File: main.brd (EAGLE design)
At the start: 78 x 235 mm, 117 parts, among them IC1 FXAS21000, IC2 ADXL343BCCZ, IC3 MPL3115A2LGA, IC4 FGPMMOPA6H, IC5 25LC1024-I/P, Q1 MCP9700A-E/TO, Q2 MCP9700A-E/TO, Q3 12MHz, Q4 FQP7P06, U1 ATMEGA1284P-PU, U2 LT3570EFEPBF, U3 TL431BQLP, X1 132134RP

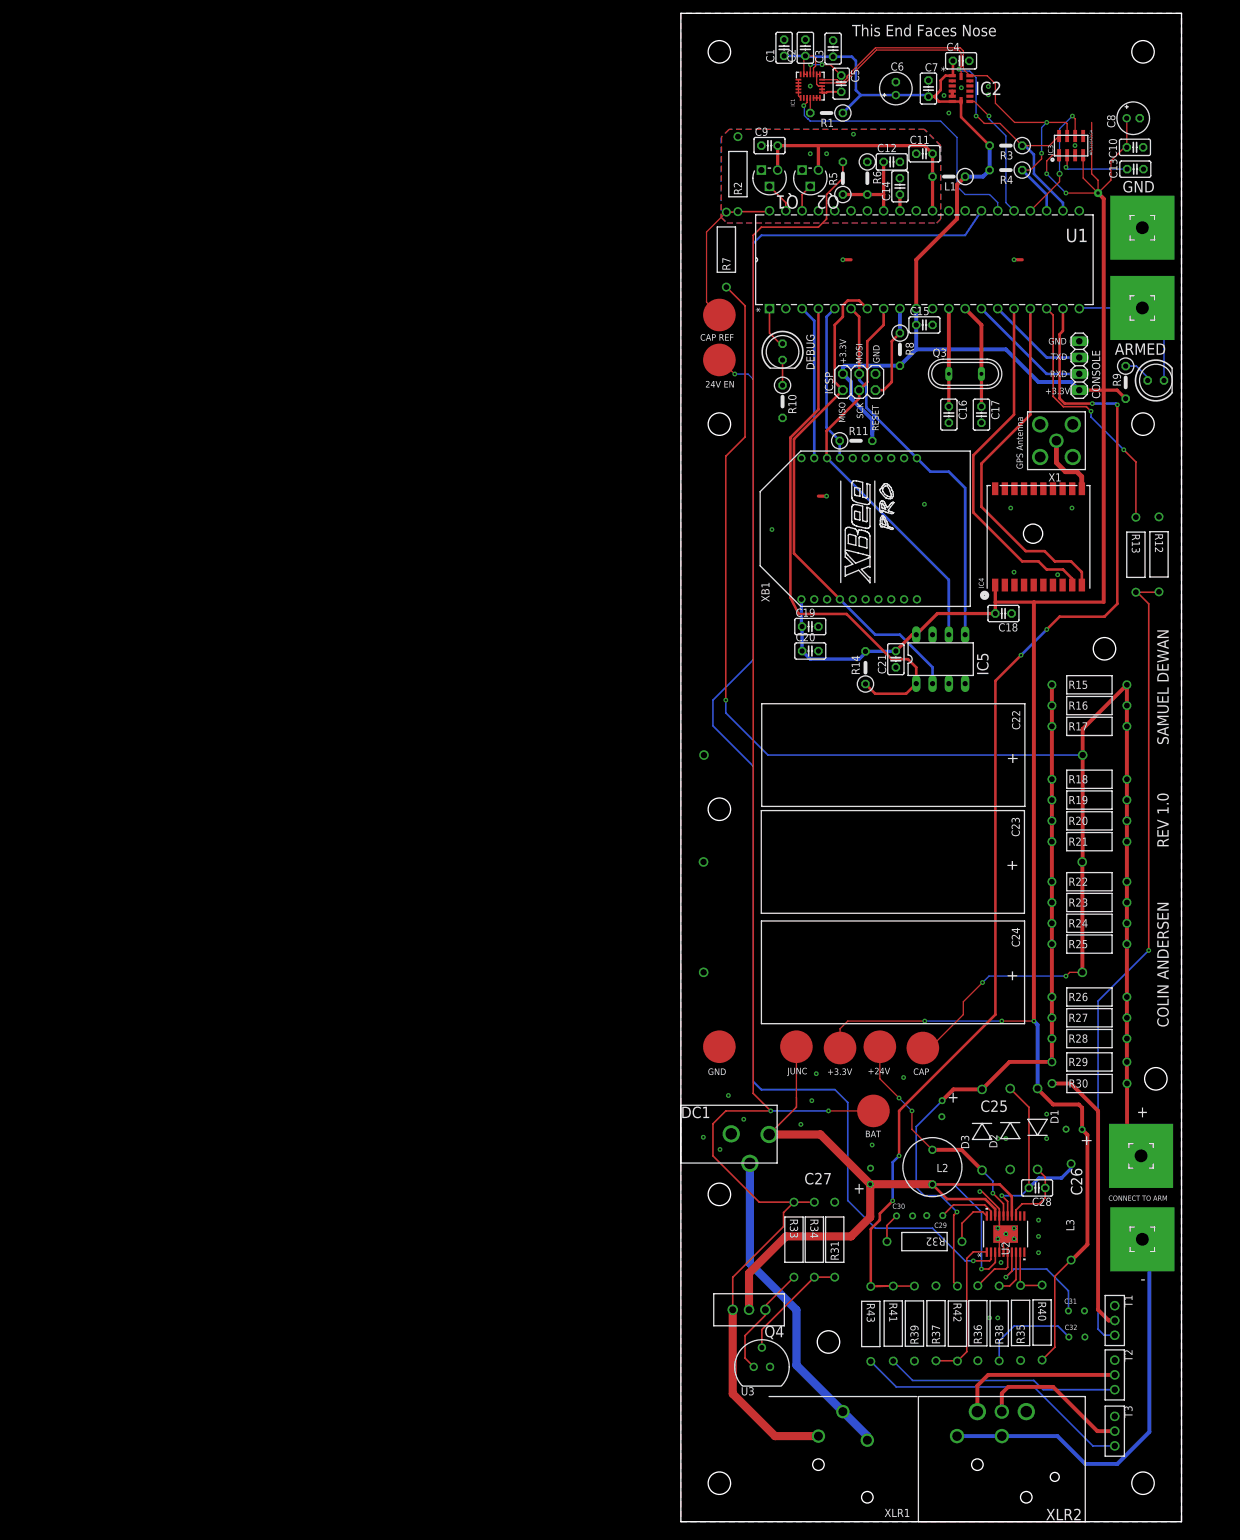
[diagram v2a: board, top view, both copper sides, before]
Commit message: Relayed-out digital section.
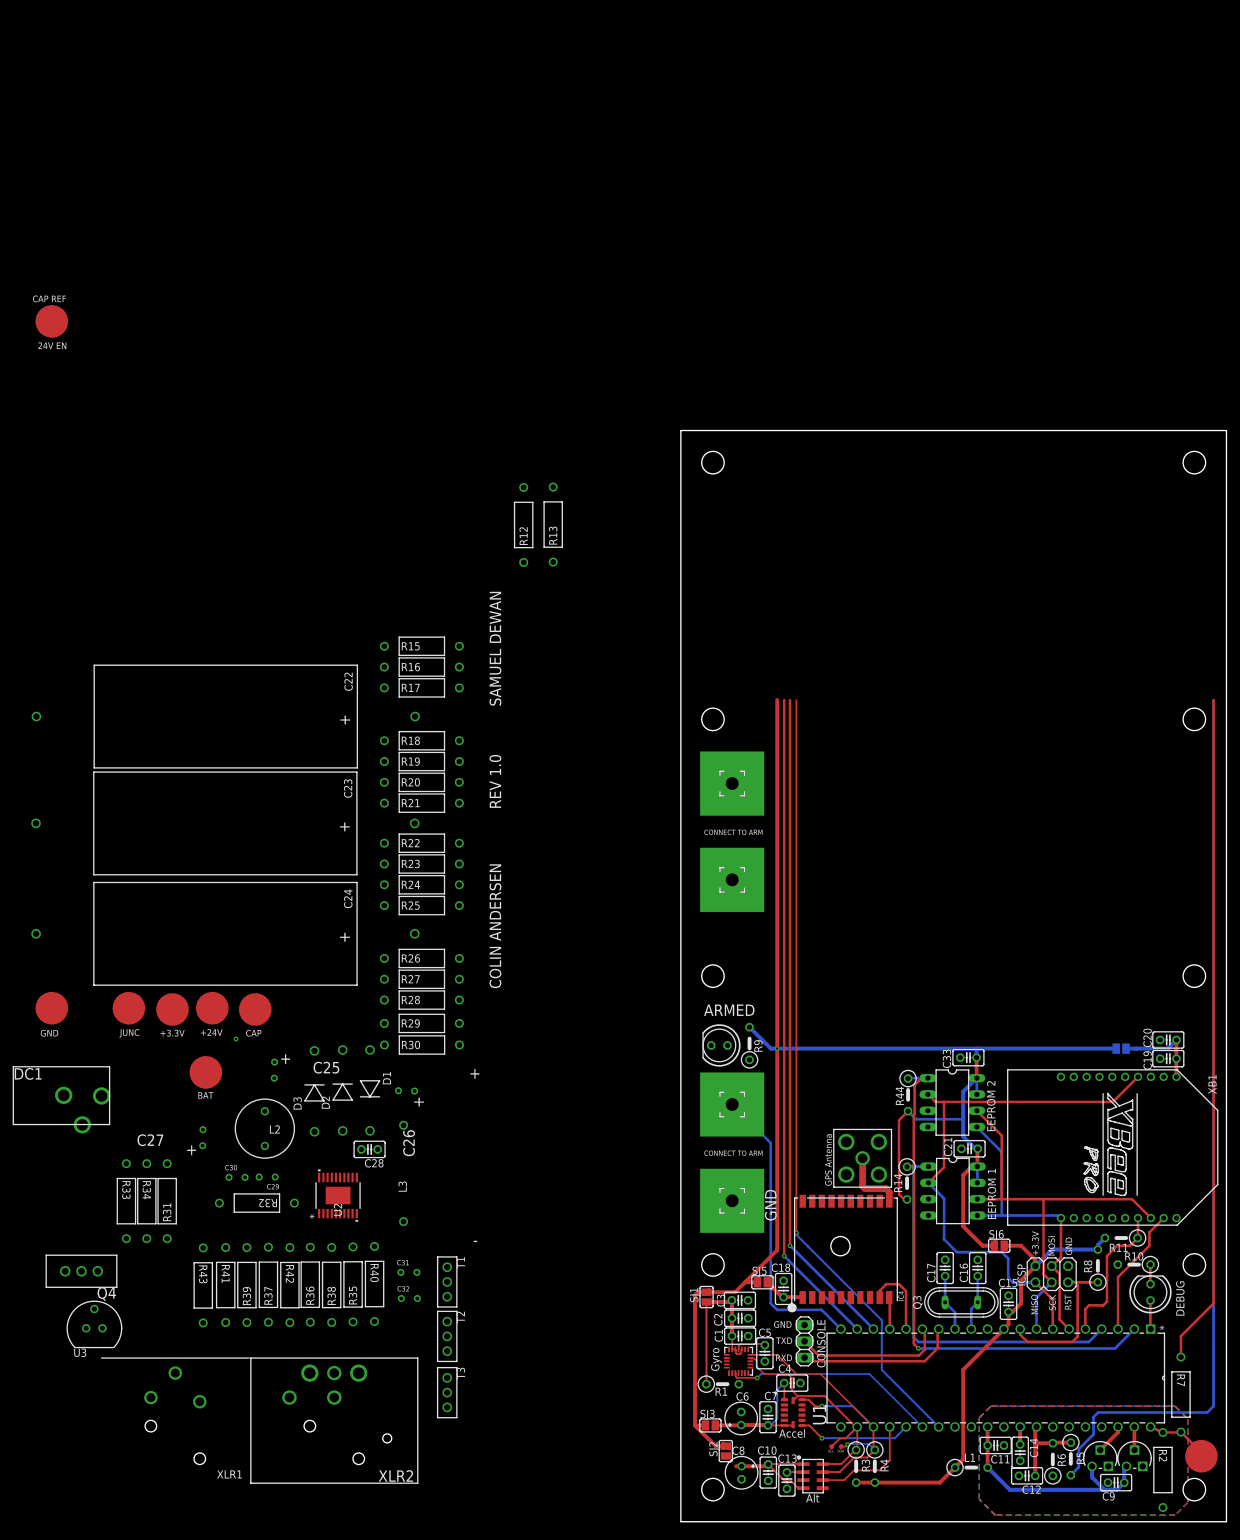
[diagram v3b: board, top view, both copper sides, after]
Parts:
- added C33: 0.1µF, rcl:C025-025X050
- added IC6: 25LC1024-I/P, microchip:DIL8
- added R44: 1MΩ, rcl:0207/5V
- added SCL, SDA: TEST-POINT3, SparkFun-Connectors:PAD.03X.03
- added SJ1, SJ2, SJ3, SJ4, SJ5, SJ6: (no value), jumper:SJ
- CONSOLE: device pinhead:1X04 -> pinhead:1X03
- R10: value 2K2Ω -> 1KΩ
- R3, R4: value 4k7Ω -> 2k2Ω
- R9: value 2K2Ω -> 180Ω
- moved R2 223.6 mm to (75.1, 2.21), turned to 270 degrees
- moved C8 219.7 mm to (9.46, 7.63), turned to 270 degrees
- moved C9 215.2 mm to (67.8, 6.09)
- moved C10 214.2 mm to (13.6, 7.65), turned to 270 degrees
- moved C13 211.4 mm to (16.5, 6.40), turned to 270 degrees
- moved IC3 211.2 mm to (20.6, 7.10), turned to 0 degrees
- moved C6 208.6 mm to (9.39, 16.1)
- moved C7 208.5 mm to (13.6, 16.3)
- moved IC2 207.9 mm to (17.5, 17.0)
- moved C4 207.7 mm to (17.4, 21.6)
- moved R3 207.1 mm to (27.3, 8.64), turned to 270 degrees
- moved C12 205.8 mm to (53.9, 7.15), turned to 180 degrees
- moved Q1 205.7 mm to (72.0, 11.2), turned to 0 degrees
- moved R4 203.0 mm to (30.2, 8.64), turned to 270 degrees
- moved R7 202.8 mm to (77.9, 14.0), turned to 270 degrees
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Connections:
- new net EEPROM2_CS: IC6.1, R44.1, U1.2
- new net RELAY_ARM: U1.27
- new net VCC_ACCEL: C4.1, C6.+, C7.1, IC2.1, IC2.6, IC2.7, SJ3.2
- new net VCC_ALT: C10.1, C8.+, IC3.P$1, IC3.P$4, SJ2.2
- new net VCC_GPS: C18.2, IC4.P$1, SJ5.2
- new net VCC_GYRO: C1.1, C2.1, C3.1, IC1.15, IC1.17, IC1.18, R1.1, SJ1.2
- new net VCC_MCU: C15.1, ICSP.2, L1.1, R11.2, R3.2, R4.2, R8.2, SJ6.2, U1.10
- new net VCC_XB: C19.1, C20.1, SJ4.2, XB1.1
- net 12V_ENABLE: no longer U1.27
- net GND: now also C33.2, CONSOLE.3, IC6.3, IC6.4; no longer CONSOLE.4, IC5.7
- net MISO: now also IC6.2
- net MOSI: now also IC6.5
- net RXD0: now also CONSOLE.1; no longer CONSOLE.2
- net SCK: now also IC6.6
- net SCL: now also SCL.P$1
- net SDA: now also SDA.P$1
- net TXD0: now also CONSOLE.2; no longer CONSOLE.3
- net VCC: now also C33.1, IC5.7, IC6.7, IC6.8, R44.2, SJ1.1, SJ2.1, SJ3.1, SJ4.1, SJ5.1, SJ6.1; no longer C1.1, C10.1, C15.1, C18.2, C19.1, C2.1, C20.1, C3.1, C4.1, C6.+, C7.1, C8.+, CONSOLE.1, IC1.15, IC1.17, IC1.18, IC2.1, IC2.6, IC2.7, IC3.P$1, IC3.P$4, IC4.P$1, ICSP.2, L1.1, R1.1, R11.2, R3.2, R4.2, R8.2, U1.10, XB1.1
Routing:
- net 12V_ENABLE: track 239.1 -> 0.00 mm, vias 2 -> 0
- net VCC: track 495.7 -> 257.9 mm, vias 6 -> 1
- net N$81: track 280.6 -> 104.5 mm, vias 3 -> 0
- net PWR_JUNC: track 128.6 -> 0.00 mm, vias 1 -> 0
- net N$82: track 125.7 -> 0.00 mm, vias 1 -> 0
- net RELAY_ARM: track 0.00 -> 122.4 mm, vias 0 -> 1
- net BAT+: track 259.5 -> 139.9 mm, vias 2 -> 0
- net +12.0: track 113.5 -> 0.00 mm, vias 1 -> 0
- net MAIN_TRIGGER: track 191.3 -> 102.7 mm, vias 6 -> 1
- net EEPROM2_CS: track 0.00 -> 81.9 mm, vias 0 -> 1
- net VCC_MCU: track 0.00 -> 73.1 mm
- net N$31: track 64.3 -> 0.00 mm
- net CAP_DISCHARGE: track 40.4 -> 103.4 mm, vias 2 -> 1
- net TXD1: track 55.9 -> 4.95 mm
- net N$30: track 50.7 -> 0.00 mm
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- removed copper zone on layer 1, net GND
- removed copper zone on layer 16, net GND
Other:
- board size 78 x 235 mm -> 85 x 170 mm
- board text added: "Accel"
- board text added: "Alt"
- board text added: "EEPROM 1"
- board text added: "EEPROM 2"
- board text added: "Gyro"
- board text added: "RST"
- board text added: "SCL"
- board text added: "SDA"
- board text removed: "RESET"
- board text removed: "This End Faces Nose"

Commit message: Update
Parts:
- removed ARMED: RED, led:LED5MM
- removed DC1: PJ-102BH, Power:DC_JACK_3
- removed PAD4: (no value), Power:3,81/1,4
- removed SJ6: (no value), jumper:SJ
- removed U$8: BAT+, Power:TEST
- added ARMED1, ARMED2: RED, led:LED5MM
- added C34: 10µF, rcl:E2-5
- added C35, C36, C37: 0.1µF, rcl:C025-025X050
- added Q5: MCP9700A-E/TO, CU in Space:TO127P254X533-3
- added R45, R48: (no value), rcl:0207/5V
- added R46, R47: 47kΩ, rcl:0207/5V
- added R49, R50: 2k2Ω, rcl:0207/5V
- added SJ200: (no value), jumper:SJ
- added T4: (no value), Power:NPNDARL
- C1, C14, C2: value 0.1µF -> 22µF; device rcl:C025-025X050 -> Power:2.5MM_AL_CAP
- C11, C4: value 0.1µF -> 338TTA035M; device rcl:C025-025X050 -> Power:338TTA035M
- C12: value 0.1µF -> SNUB
- C13, C3, C7: value 0.1µF -> 10 uF; device rcl:C025-025X050 -> Power:2.5MM_CAP
- C15: value 2.2µF -> 338TTA035M; device rcl:C025-025X050 -> Power:338TTA035M
- C16: value 27pF -> 1µF
- C17: value 27pF -> 0.1µF
- C18: value 0.1µF -> 47pF
- C19: value 47pF -> 0.1µF
- C20: value 1µF -> 27pF
- C21: value 0.1µF -> 27pF
- C22, C23: value 338TTA035M -> 0.1µF; device Power:338TTA035M -> rcl:C025-025X050
- C24: value 338TTA035M -> 2.2µF; device Power:338TTA035M -> rcl:C025-025X050
- C25, C26, C27: value 22µF -> 0.1µF; device Power:2.5MM_AL_CAP -> rcl:C025-025X050
- C29, C31: value 10nF -> 0.1µF; device Power:2.5MM_CAP -> rcl:C025-025X050
- C30: value 1nF -> 10µF; device Power:2.5MM_CAP -> rcl:E2-5
- C32: value 1nF -> 0.1µF; device Power:2.5MM_CAP -> rcl:C025-025X050
- C5, C9: value 0.1µF -> 1nF; device rcl:C025-025X050 -> Power:2.5MM_CAP
- C6, C8: value 10µF -> 10nF; device rcl:E2-5 -> Power:2.5MM_CAP
- IC1: value FXAS21000 -> 25LC1024-I/P; device Freescale_Sensors_v2:QFN24_0P5_4X4_ASYM_EXP -> microchip:DIL8
- IC2: value ADXL343BCCZ -> 25LC1024-I/P; device CU in Space:LGA14R80P1X6_300X500X100 -> microchip:DIL8
- IC3: value MPL3115A2LGA -> FGPMMOPA6H; device microbuilder:LGA8 -> microbuilder:FGPMMOPA6H
- IC4: value FGPMMOPA6H -> FXAS21000; device microbuilder:FGPMMOPA6H -> Freescale_Sensors_v2:QFN24_0P5_4X4_ASYM_EXP
- IC5: value 25LC1024-I/P -> ADXL343BCCZ; device microchip:DIL8 -> CU in Space:LGA14R80P1X6_300X500X100
- IC6: value 25LC1024-I/P -> MPL3115A2LGA; device microchip:DIL8 -> microbuilder:LGA8
- L1: value 10µH -> 18µH; device rcl:0207/5V -> Power:5.4MM_L
- L3: value 4.7µH -> 10µH; device Power:14MM_L -> rcl:0207/5V
- Q1, Q2: value MCP9700A-E/TO -> FQP7P06; device CU in Space:TO127P254X533-3 -> Power:PMOS
- Q4: value FQP7P06 -> MCP9700A-E/TO; device Power:PMOS -> CU in Space:TO127P254X533-3
- R1: value 47kΩ -> 3.65 kΩ
- R10: value 1KΩ -> 51.1 kΩ
- R11: value 1MΩ -> BOOSTR
- R12: value 1M -> 1.2 k; device Power:YAG_MF25 -> rcl:0207/5V
- R13: value 3.6k -> SNUB; device Power:YAG_MF25 -> rcl:0207/5V
- R14: value 1MΩ -> 3.6k
- R15: value 750 -> 1.2 k; device Power:YAG_MF25 -> rcl:0207/5V
- R16: value 750 -> 3.6 k; device Power:YAG_MF25 -> rcl:0207/5V
- R17, R19: value 750 -> 1 M; device Power:YAG_MF25 -> rcl:0207/5V
- R18: value 750 -> 3.6 K; device Power:YAG_MF25 -> rcl:0207/5V
- R2: value (none) -> 1 MΩ; device Power:YAG_MF25 -> rcl:0207/5V
- R20: value 750 -> 1.4 k; device Power:YAG_MF25 -> rcl:0207/5V
- R21, R22, R23, R24, R25, R26, R27, R28: value 750 -> (none); device Power:YAG_MF25 -> rcl:0207/5V
- R29: value 750 -> 2M Ω; device Power:YAG_MF25 -> rcl:0207/5V
- R3: value 2k2Ω -> 1 MΩ
- R30: value ~1.4k -> 1MΩ; device Power:YAG_MF25 -> rcl:0207/5V
- R31, R34, R40: value 51.1kΩ -> (none); device Power:YAG_MF25 -> rcl:0207/5V
- R32: value 24.9kΩ -> 1.2 k; device Power:YAG_MF25 -> rcl:0207/5V
- R33: value 3.65kΩ -> 1.2k; device Power:YAG_MF25 -> rcl:0207/5V
- R35: value 17.4kΩ -> (none); device Power:YAG_MF25 -> rcl:0207/5V
- R36: value 8.06kΩ -> (none); device Power:YAG_MF25 -> rcl:0207/5V
- R37: value 3.65kΩ -> 1MΩ; device Power:YAG_MF25 -> rcl:0207/5V
- R38: value 24.9kΩ -> (none); device Power:YAG_MF25 -> rcl:0207/5V
- R39: value 1M -> (none); device Power:YAG_MF25 -> rcl:0207/5V
- R4: value 2k2Ω -> 51.1 kΩ
- R41: value 3.6k -> 1MΩ; device Power:YAG_MF25 -> rcl:0207/5V
- R42: value 51.1kΩ -> 1KΩ; device Power:YAG_MF25 -> rcl:0207/5V
- R43: value 3.6k -> 10kΩ; device Power:YAG_MF25 -> rcl:0207/5V
- R44: value 1MΩ -> 47kΩ
- R5: value 47kΩ -> 373.65 kΩ
- R6: value 47kΩ -> 24.9 kΩ
- R7: value (none) -> 8.06 kΩ; device Power:YAG_MF25 -> rcl:0207/5V
- R8: value 10kΩ -> 24.9 kΩ
- R9: value 180Ω -> 17.4 kΩ
- U$1: value TEST -> BAT+
- U$2: value TEST -> +24V
- U$3: value CAP -> +3.3V
- U$4: value BAT+ -> CAP
- U$5: value +24V -> TEST
- U$6: value +3.3V -> CAP
- U$7: value CAP -> TEST
- U1: value ATMEGA1284P-PU -> TL431BQLP; device Atmel_By_element14_Batch_1-00:DIP254P1524X483-40 -> Power:LP3
- U3: value TL431BQLP -> ATMEGA1284P-PU; device Power:LP3 -> Atmel_By_element14_Batch_1-00:DIP254P1524X483-40
- moved XLR1 186.7 mm to (39.4, 150.5)
- moved XLR2 186.5 mm to (64.1, 150.4)
- moved R2 169.5 mm to (6.00, 157.0), turned to 0 degrees
- moved Q1 162.9 mm to (22.3, 166.3)
- moved Q4 162.4 mm to (66.6, 11.2), turned to 0 degrees
- moved C24 156.9 mm to (51.0, 33.9), turned to 90 degrees
- moved U$7 154.6 mm to (79.1, 27.2), turned to 90 degrees
- moved U1 151.7 mm to (11.1, 165.8), turned to 180 degrees
- moved R5 148.7 mm to (6.00, 148.0), turned to 0 degrees
- moved R3 146.9 mm to (6.00, 154.0), turned to 180 degrees
- moved R6 144.9 mm to (6.00, 145.0), turned to 0 degrees
- moved C9 144.9 mm to (6.70, 137.5), turned to 180 degrees
- moved C22 144.8 mm to (16.0, 36.3)
- moved R4 144.4 mm to (6.00, 151.0), turned to 180 degrees
- moved R7 144.2 mm to (6.00, 139.0), turned to 0 degrees
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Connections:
- removed net ARMED_SENSE: ARMED.K, PAD2.1, U1.20
- removed net N$33: ARMED.A, R9.1
- removed net RELAY_ARM: U1.27
- new net EMATCH_SENSE_1: ARMED1.K, R33.1, U3.20
- new net EMATCH_SENSE_2: ARMED2.K, R32.1, U3.21
- new net N$35: R24.2, T4.3
- new net N$67: C12.1, R13.1
- new net N$75: C10.1, R11.1
- new net N$84: ARMED2.A, R15.2
- new net N$85: ARMED1.A, R12.1
- net +12.0: now also C2.1, C3.1, D1.1, R31.1, R34.1, R35.1, R36.1, R38.1, R39.1, R4.1, R40.1, U$2.P$1; no longer C25.1, D3.1, R15.1, R16.1, R17.1, R18.1, R19.1, R20.1, R21.1, R24.1, R29.1, R42.1
- net 12V_ENABLE: now also R24.1, R29.2, U$5.P$1, U3.27; no longer U$2.P$1
- net ACCEL_INT: now also IC5.8, U3.25; no longer IC2.8, U1.25
- net ALT_INT: now also IC6.P$6, U3.24; no longer IC3.P$6, U1.24
- net AREF: now also C32.1, U3.32; no longer C14.1, U1.32
- net AVCC: now also C31.2, C37.2, L3.2, Q4.1, Q5.1, U3.30; no longer C11.2, C9.2, L1.2, Q1.1, Q2.1, U1.30
- net A_GND: now also C31.1, C32.2, C35.2, C37.1, Q4.3, Q5.3, R47.1, R48.2, U3.31; no longer C11.1, C12.2, C14.2, C9.1, Q1.3, Q2.3, R2.2, R6.1, U1.31
- net BAT+: now also Q1.3, R1.1, R2.1, R46.2, U$1.P$1; no longer Q4.3, R33.1, R34.1, R5.2, U$8.P$1
- net BAT_REF: now also C35.1, R46.1, R47.2, U3.33; no longer C12.1, R5.1, R6.2, U1.33
- net CAP_DISCHARGE: now also R18.1, U3.18; no longer R13.1, U1.18
- net CAP_REF: now also R45.2, R48.1, U$7.P$1, U3.40; no longer R2.1, R7.2, U$1.P$1, U1.40
- net DEBUG_LED: now also U3.1; no longer U1.1
- net EEPROM2_CS: now also IC1.1, R30.1, U3.2; no longer IC6.1, R44.1, U1.2
- net EEPROM_CS: now also IC2.1, R37.1, U3.4; no longer IC5.1, R14.1, U1.4
- net FB1: now also R4.2, R5.1; no longer R37.1, R42.2
- net GND: now also C11.-, C12.2, C14.2, C15.-, C18.2, C22.1, C23.2, C24.2, C28.2, C30.-, C34.-, C36.2, C4.-, C6.2, C8.2, C9.2, IC1.3, IC1.4, IC2.3, IC3.P$12, IC3.P$19, IC3.P$8, IC4.1, IC4.10, IC4.13, IC4.14, IC4.19, IC4.20, IC4.21, IC4.22, IC4.23, IC4.24, IC4.5, IC4.6, IC4.7, IC4.8, IC4.9, IC5.12, IC5.2, IC5.5, IC6.P$3, R17.1, R19.1, R29.1, R3.2, R32.2, R33.2, R42.2, R5.2, R7.1, R9.1, T4.1, U$4.P$1, U1.3, U3.11, XLR1.1, XLR1.3; no longer C10.2, C15.2, C18.1, C22.-, C23.-, C24.-, C30.2, C31.2, C32.2, C4.2, C6.-, C8.-, DC1.2, IC1.1, IC1.10, IC1.13, IC1.14, IC1.19, IC1.20, IC1.21, IC1.22, IC1.23, IC1.24, IC1.5, IC1.6, IC1.7, IC1.8, IC1.9, IC2.12, IC2.2, IC2.5, IC4.P$12, IC4.P$19, IC4.P$3, IC4.P$8, IC5.3, IC6.3, IC6.4, PAD1.1, R10.2, R12.1, R31.2, R35.1, R36.1, R37.2, R39.1, U$3.P$1, U1.11, U3.3
- net GPS_FIX: now also IC3.P$5; no longer IC4.P$5
- net GYRO_INT: now also IC4.3, U3.26; no longer IC1.3, U1.26
- net MAIN_TRIGGER: now also R14.1, R16.1, R17.2, U3.19; no longer R39.2, R41.1, R43.1, U1.19
- net MISO: now also IC1.2, IC2.2, U3.7; no longer IC5.2, IC6.2, U1.7
- net MOSI: now also IC1.5, IC2.5, U3.6; no longer IC5.5, IC6.5, U1.6
- net N$1: now also C27.1, IC4.16; no longer C5.1, IC1.16
- net N$10: now also C9.1, R8.1; no longer C32.1, R38.1
- net N$11: now also R6.1; no longer R32.1
- net N$12: now also C6.1; no longer C29.1
- net N$13: now also C10.2, L2.1, R13.2; no longer C28.2, L3.1
- net N$15: now also R10.1, R9.2; no longer R35.2, R40.1
- net N$16: now also D3.1, R11.2; no longer C28.1, D1.1
- net N$2: now also IC4.4, R44.2; no longer IC1.4, R1.2
- net N$3: now also C36.1, IC6.P$2; no longer C13.1, IC3.P$2
- net N$30: now also Q2.3, R21.1, R22.2, R23.2, R25.2, R26.2, R27.2, R28.2, R31.2, R34.2, R35.2, R36.2, R38.2, R39.2, R40.2; no longer DC1.3, XLR1.1, XLR1.3
- net N$31: now also Q2.1, R21.2, T4.2; no longer PAD4.1, XLR2.1, XLR2.3
- net N$34: now also R20.2, T3.2; no longer R30.1, T1.2
- net N$4: now also IC3.P$11; no longer IC4.P$11
- net N$5: now also C8.1; no longer C31.1
- net N$6: now also R7.2; no longer R36.2
- net N$69: now also Q1.1, R1.2, U1.1; no longer Q4.1, R33.2, U3.1
- net N$7: now also R8.2; no longer R38.2
- net N$70: now also R2.2, R3.1, U1.2; no longer R31.1, R34.2, U3.2
- net N$71: now also R42.1; no longer R10.1
- net N$77: now also PAD3.1, R15.1, T1.2, XLR2.4; no longer T3.2, XLR2.2
- net N$78: now also PAD2.1, R12.2, XLR2.3; no longer XLR2.4
- net N$79: now also R16.2, T2.3; no longer R43.2, T3.3
- net N$8: now also D1.2, L1.2; no longer D3.2, L2.2, U$5.P$1
- net N$80: now also R14.2, T1.3; no longer R41.2, T2.3
- net N$81: now also C11.+, C15.+, C4.+, PAD1.1, Q2.2, R20.1, R45.1, U$6.P$1, XLR2.1, XLR2.2; no longer C22.+, C23.+, C24.+, PAD3.1, R15.2, R16.2, R17.2, R18.2, R19.2, R20.2, R21.2, R22.2, R23.2, R24.2, R25.2, R26.2, R27.2, R28.2, R29.2, R30.2, R7.1, U$7.P$1
- net N$82: now also R18.2, R19.2, T3.3; no longer R12.2, R13.2, T1.3
- net N$9: now also C5.1, R6.2; no longer C30.1, R32.2
- net PWR_JUNC: now also C1.1, C7.1, L1.1, Q1.2; no longer C27.1, DC1.1, L2.1, Q4.2, U$4.P$1
- net RADIO_CS: now also R41.1, U3.5; no longer R11.1, U1.5
- net RADIO_INT: now also U3.3; no longer U1.3
- net RESET: now also R43.1, U3.9; no longer R8.1, U1.9
- net RXD0: now also U3.14; no longer U1.14
- net RXD1: now also IC3.P$9, U3.16; no longer IC4.P$9, U1.16
- net SCK: now also IC1.6, IC2.6, U3.8; no longer IC5.6, IC6.6, U1.8
- net SCL: now also IC4.11, IC5.14, IC6.P$8, R49.1, U3.22; no longer IC1.11, IC2.14, IC3.P$8, R3.1, U1.22
- net SDA: now also IC4.12, IC5.13, IC6.P$7, R50.1, U3.23; no longer IC1.12, IC2.13, IC3.P$7, R4.1, U1.23
- net TEMP: now also Q5.2, U3.39; no longer Q1.2, U1.39
- net TEMP2: now also Q4.2, U3.38; no longer Q2.2, U1.38
- net TXD0: now also U3.15; no longer U1.15
- net TXD1: now also IC3.P$10, U3.17; no longer IC4.P$10, U1.17
- net VCC: now also C13.1, C14.1, C17.1, C19.1, D3.2, IC1.7, IC1.8, IC2.7, IC2.8, L2.2, R10.2, R30.2, R37.2, SJ200.1, U$3.P$1; no longer C21.1, C26.1, C33.1, D1.2, IC5.7, IC5.8, IC6.7, IC6.8, L3.2, R14.2, R40.2, R44.2, R9.2, SJ6.1, U$6.P$1
- net VCC_ACCEL: now also C28.1, C29.1, C30.+, IC5.1, IC5.6, IC5.7, SJ4.2; no longer C4.1, C6.+, C7.1, IC2.1, IC2.6, IC2.7, SJ3.2
- net VCC_ALT: now also C33.1, C34.+, IC6.P$1, IC6.P$4, SJ5.2; no longer C10.1, C8.+, IC3.P$1, IC3.P$4, SJ2.2
- net VCC_GPS: now also C22.2, IC3.P$1, SJ2.2; no longer C18.2, IC4.P$1, SJ5.2
- net VCC_GYRO: now also C23.1, C25.1, C26.1, IC4.15, IC4.17, IC4.18, R44.1, SJ3.2; no longer C1.1, C2.1, C3.1, IC1.15, IC1.17, IC1.18, R1.1, SJ1.2
- net VCC_MCU: now also C24.1, L3.1, R41.2, R43.2, R49.2, R50.2, SJ1.2, U3.10; no longer C15.1, L1.1, R11.2, R3.2, R4.2, R8.2, SJ6.2, U1.10
- net VCC_XB: now also C16.1, C18.1, SJ200.2; no longer C19.1, C20.1, SJ4.2
- net XTAL1: now also C20.1, U3.13; no longer C17.1, U1.13
- net XTAL2: now also C21.1, U3.12; no longer C16.1, U1.12
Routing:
- net +12.0: track 0.00 -> 216.4 mm, vias 0 -> 2
- net N$81: track 104.5 -> 303.0 mm
- net BAT+: track 139.9 -> 307.9 mm, vias 0 -> 4
- net 12V_ENABLE: track 0.00 -> 157.4 mm, vias 0 -> 4
- net EMATCH_SENSE_2: track 0.00 -> 151.1 mm, vias 0 -> 8
- net EMATCH_SENSE_1: track 0.00 -> 131.5 mm, vias 0 -> 4
- net N$77: track 0.00 -> 129.6 mm, vias 0 -> 3
- net RELAY_ARM: track 122.4 -> 0.00 mm, vias 1 -> 0
- net N$78: track 0.00 -> 117.2 mm
- net PWR_JUNC: track 0.00 -> 87.7 mm, vias 0 -> 1
- net N$30: track 0.00 -> 69.2 mm
- net GND: track 0.00 -> 59.6 mm, vias 0 -> 449
- net ARMED_SENSE: track 46.1 -> 0.00 mm
- net N$8: track 0.00 -> 35.8 mm
- net N$13: track 0.00 -> 33.4 mm
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- added copper zone on layer 1, net GND
- added copper zone on layer 16, net GND
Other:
- board text added: "2018 HARDWARE & SOFTWARE TEAM: ANDREW DION APEKSHA BUDHKAR COLIN ANDERSEN CAMERON SOMERS FEDERICO NARANJO JOREN RAYMOND MICHAEL AZIZ MICHAEL WIEBE RAFI KHAN SAMUEL DEWAN TADHG MCDONALD-JENSEN ZHONGTIAN XIA"
- board text added: "ARMED 1"
- board text added: "ARMED 2"
- board text added: "C:/Users/Colin/Desktop/inspacetest.bmp"
- board text added: "REV 2.0"
- board text removed: "+"
- board text removed: "+24V"
- board text removed: "-"
- board text removed: "24V EN"
- board text removed: "BAT"
- board text removed: "CAP"
- board text removed: "CAP REF"
- board text removed: "JUNC"
- board text removed: "REV 1.0"
